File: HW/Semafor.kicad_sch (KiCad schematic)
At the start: 27 parts, among them J1 USB_C_Receptacle_USB2.0, U1 ESP32-C3

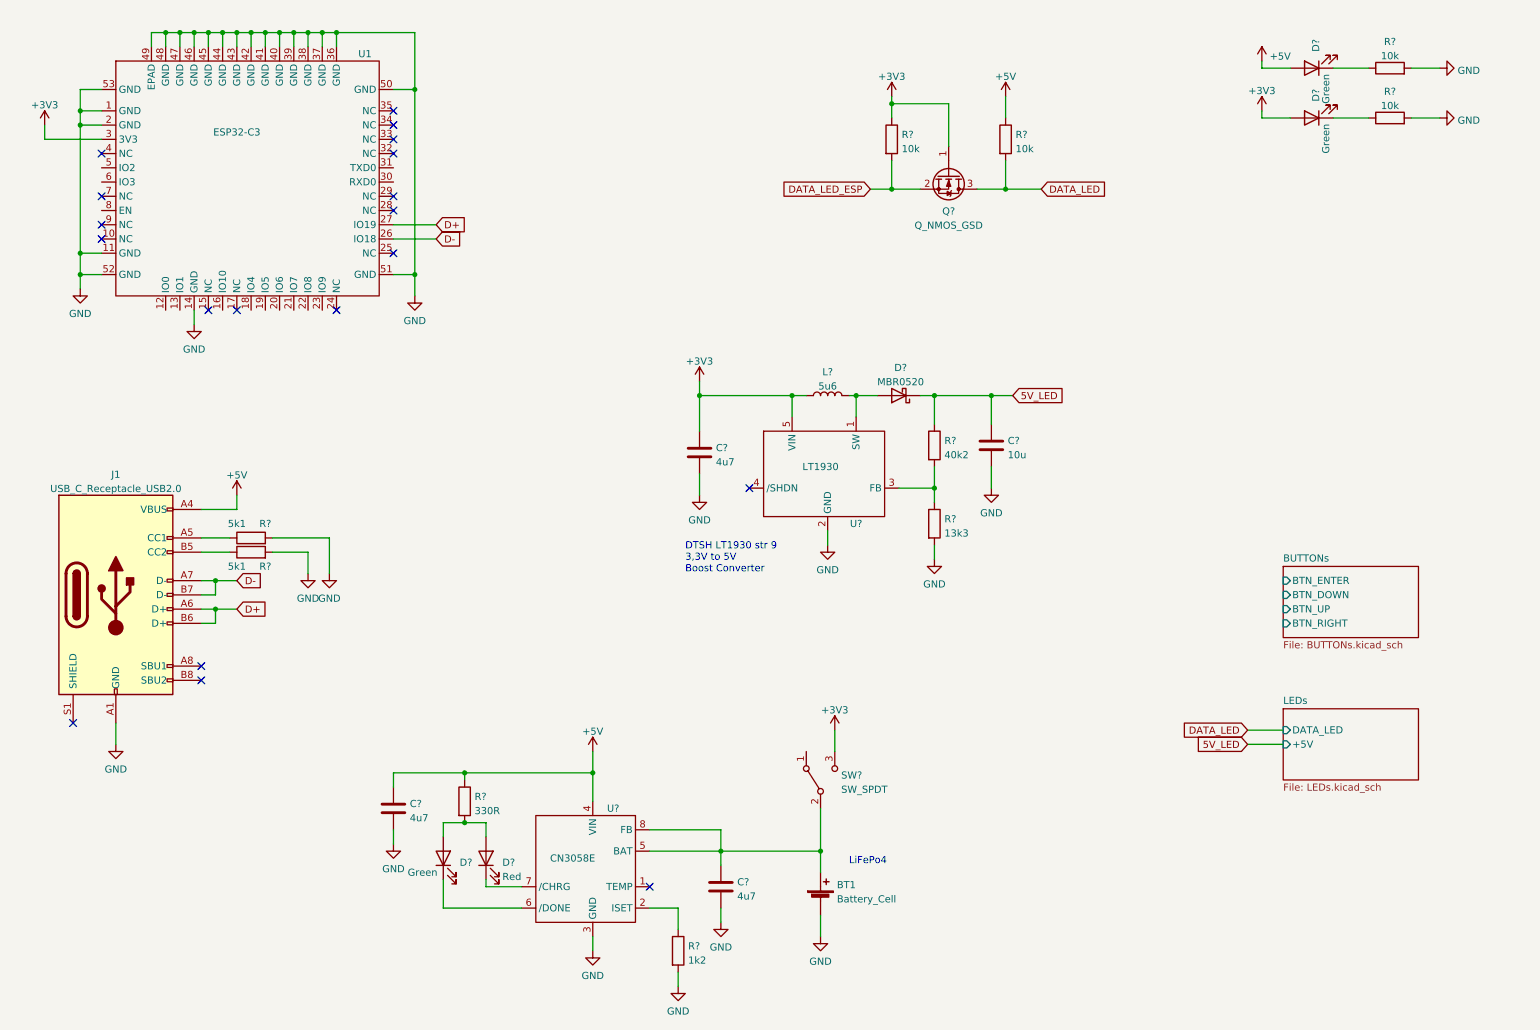
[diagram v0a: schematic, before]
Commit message: add peripherial for ESP32-C3, add temporary package of switch and inductor, add package of MOS
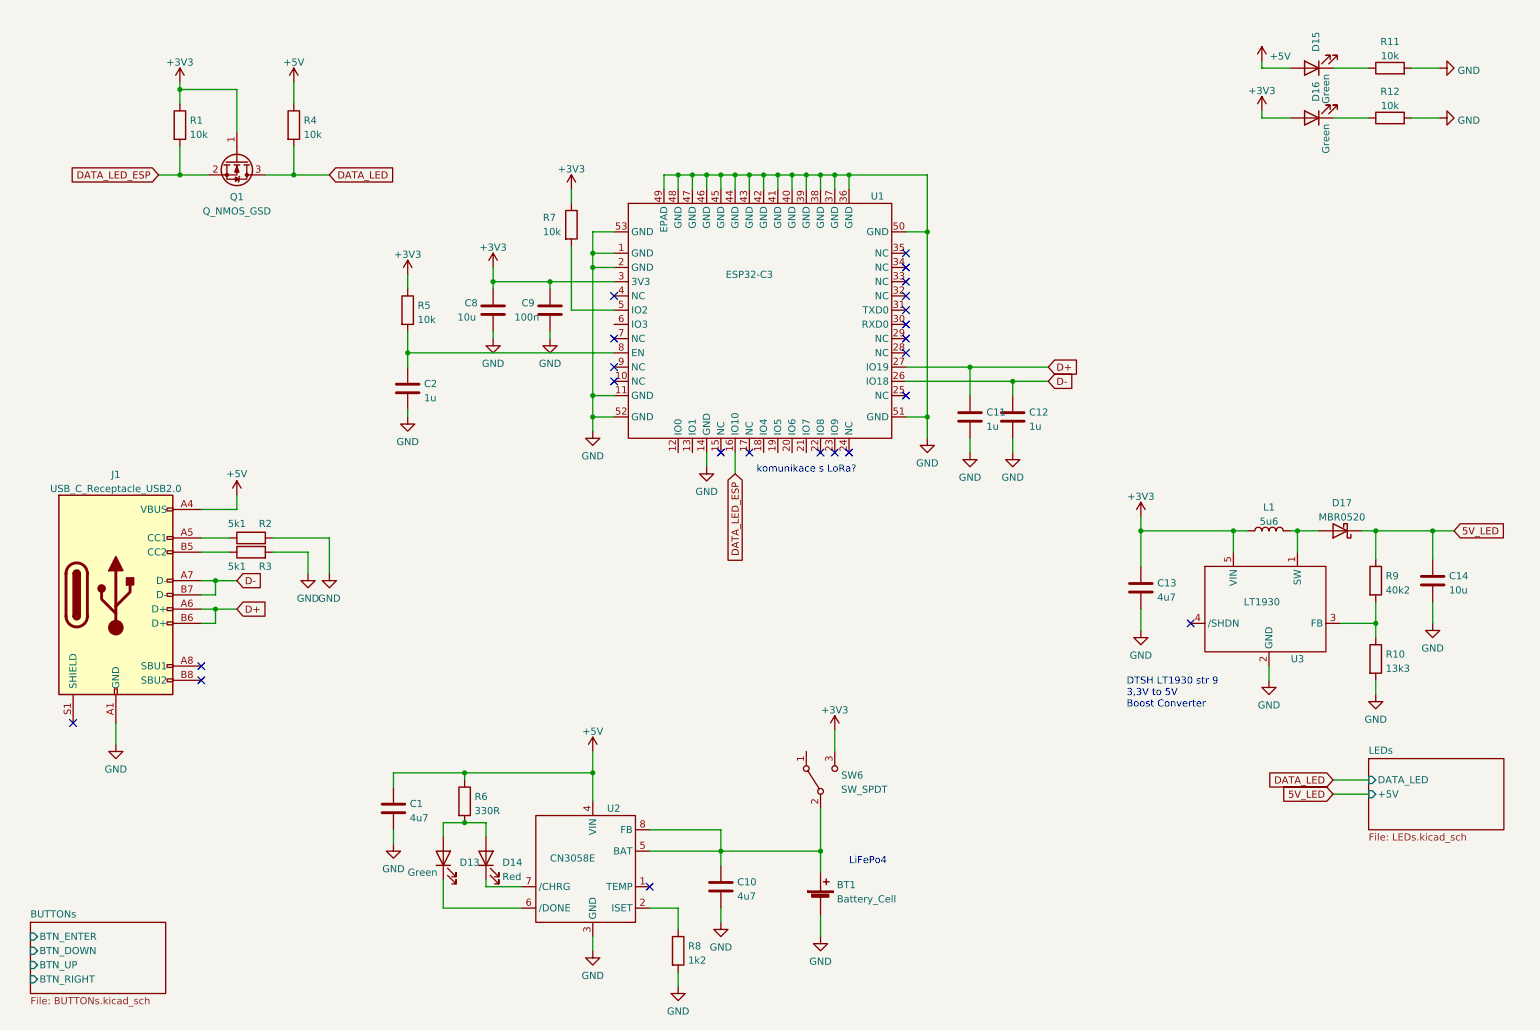
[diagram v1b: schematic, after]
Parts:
- added C11, C12, C2: 1u, Capacitor_SMD:C_0805_2012Metric, symbol Device:C
- added C8: 10u, Capacitor_SMD:C_0805_2012Metric, symbol Device:C
- added C9: 100n, Capacitor_SMD:C_0805_2012Metric, symbol Device:C
- added R5, R7: 10k, Resistor_SMD:R_0603_1608Metric, symbol Device:R
- L1: renamed from L?; footprint (none) -> Inductor_SMD:L_6.3x6.3_H3
- Q1: renamed from Q?; footprint (none) -> Package_TO_SOT_SMD:SOT-23; LCSC (none) -> C8545
- SW6: renamed from SW?; footprint (none) -> Connector_PinSocket_2.54mm:PinSocket_1x03_P2.54mm_Vertical
- gave numbers to parts that had none: 21
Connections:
- net +3V3: now also C8.1, C9.1, R5.1, R7.1
- net D+: now also C11.1
- net D-: now also C12.1
- net DATA_LED_ESP: now also U1.16 (IO10)
- net GND: now also C11.2, C12.2, C2.2, C8.2, C9.2
- net at U1.5 (IO2): now also R7.2
- net at U1.8 (EN): now also C2.1, R5.2
- no-connect marks 19 -> 23
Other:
- note added: "komunikace s LoRa?"
- moved on the sheet: C13, C14, D17, L1, Q1, R1, R10, R4, R9, U1, U3

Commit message: change package of inductor + add LSCS code
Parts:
- L1: LCSC (none) -> C167273
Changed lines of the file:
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@@
+      (effects (font (size 1.27 1.27)) hide)
+    )
+    (property "LCSC" "C167273" (id 4) (at 238.76 107.95 0)
       (effects (font (size 1.27 1.27)) hide)
     )

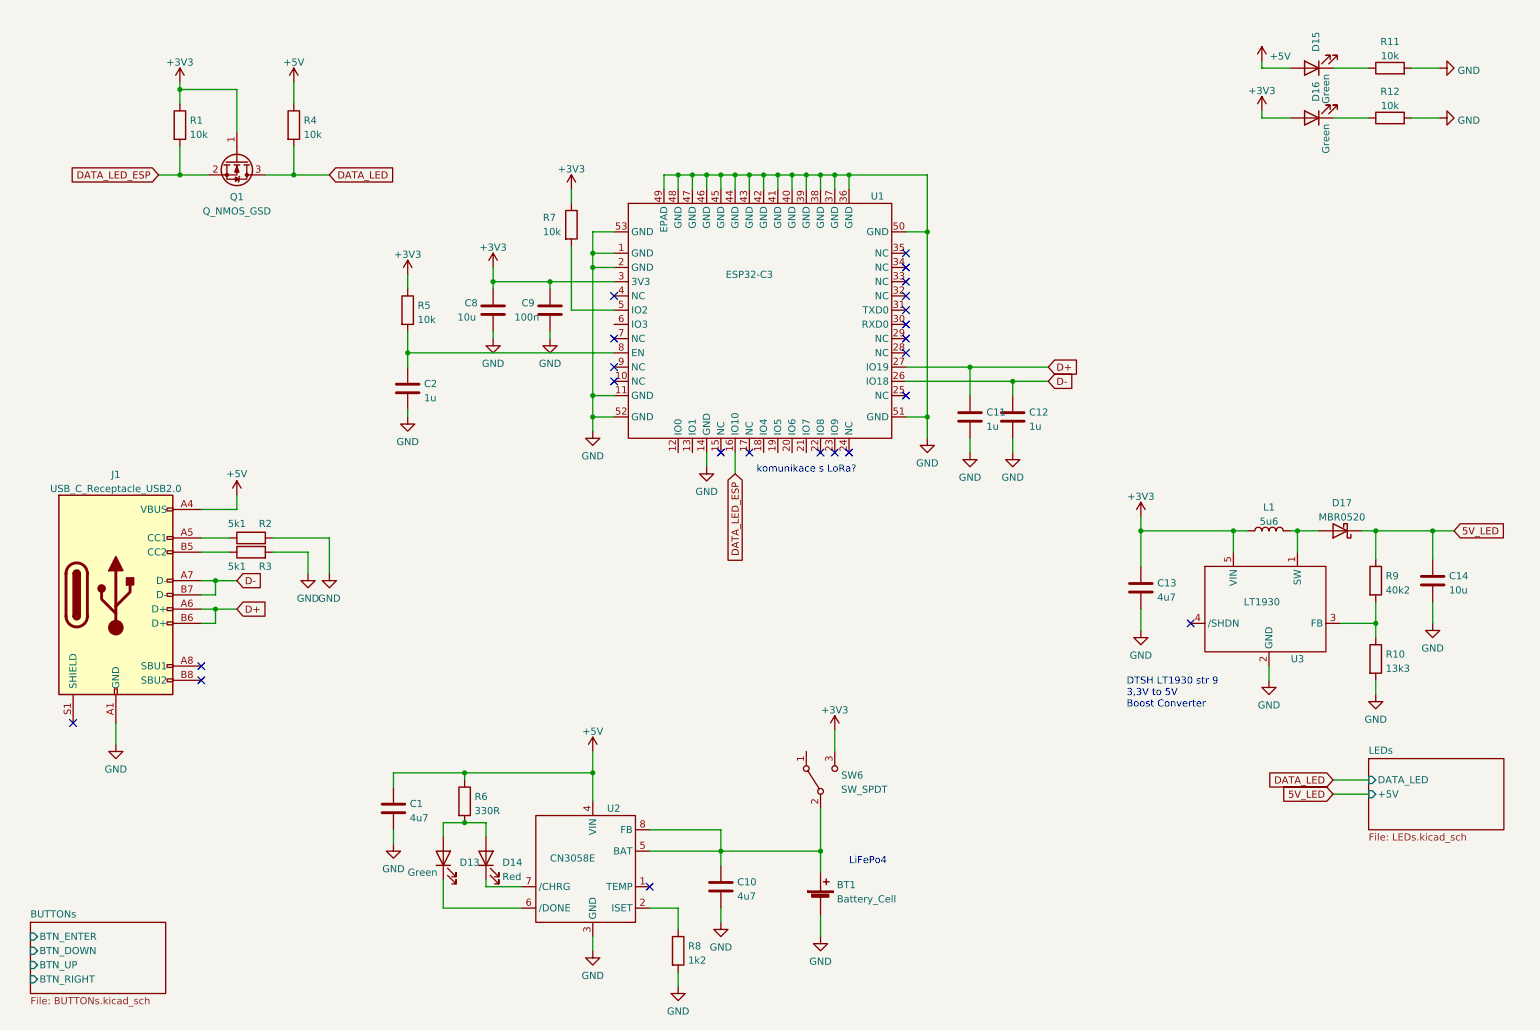
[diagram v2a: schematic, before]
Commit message: change value of inductor, update PCB, repair connection step up of pin /SHDN, delete capacitors from ESP32
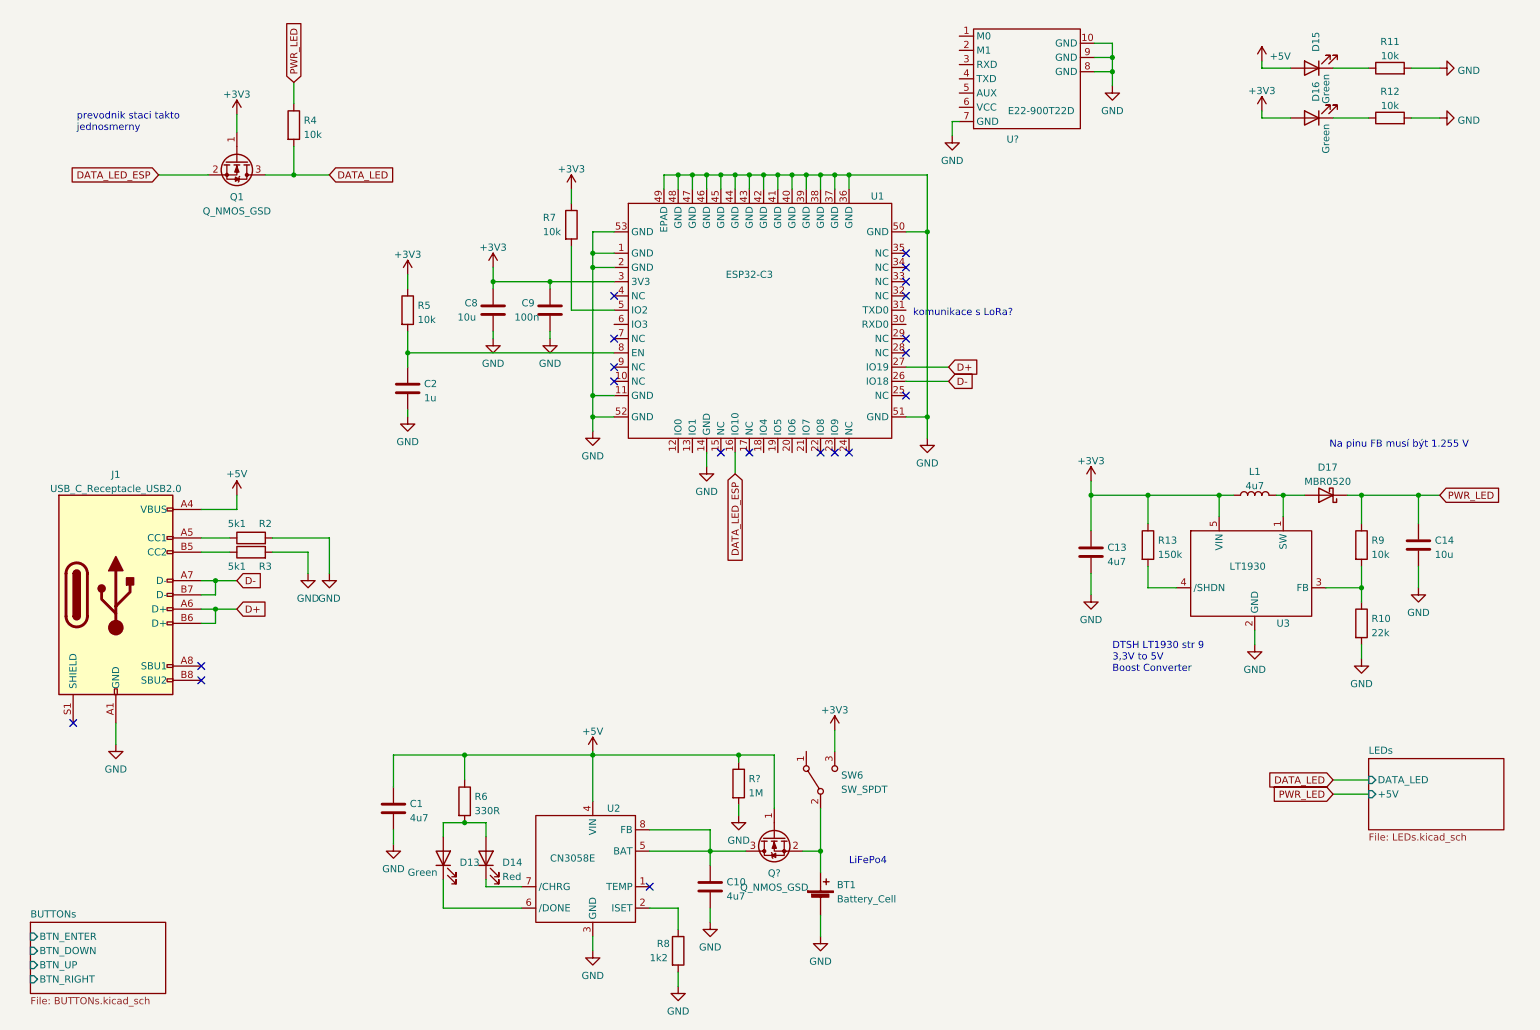
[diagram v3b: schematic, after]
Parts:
- removed C11, C12: 1u, Capacitor_SMD:C_0805_2012Metric, symbol Device:C
- removed R1: 10k, Resistor_SMD:R_0603_1608Metric, symbol Device:R
- added Q?: Q_NMOS_GSD, Package_TO_SOT_SMD:SOT-23, symbol Device:Q_NMOS_GSD
- added R13: 150k, Resistor_SMD:R_0603_1608Metric, symbol Device:R
- added R?: 1M, Resistor_SMD:R_0603_1608Metric, symbol Device:R
- added U?: E22-900T22D, Library:E22-900T22D, symbol Library:E22-900T22D
- L1: value 5u6 -> 4u7; footprint Inductor_SMD:L_6.3x6.3_H3 -> Library:L_CDRH3D18
- R10: value 13k3 -> 22k
- R9: value 40k2 -> 10k
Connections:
- net +3V3: now also R13.1
- net +5V: now also Q?.1 (G), R?.1; no longer R4.1
- net GND: now also R?.2, U?.10 (GND), U?.7 (GND), U?.8 (GND), U?.9 (GND)
- net at U3.4 (/SHDN): now also R13.2
- net at C10.1, U2.5 (BAT), U2.8 (FB): now also Q?.3 (D); no longer BT1.1 (+), SW6.2 (B)
- net 5V_LED renamed PWR_LED
- net PWR_LED: now also R4.1
- new net: BT1.1 (+), Q?.2 (S), SW6.2 (B)
- no-connect marks 23 -> 20
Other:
- note added: "Na pinu FB musí být 1.255 V"
- note added: "prevodnik staci takto jednosmerny"
- moved on the sheet: C10, C13, C14, D17, L1, R10, R9, U3

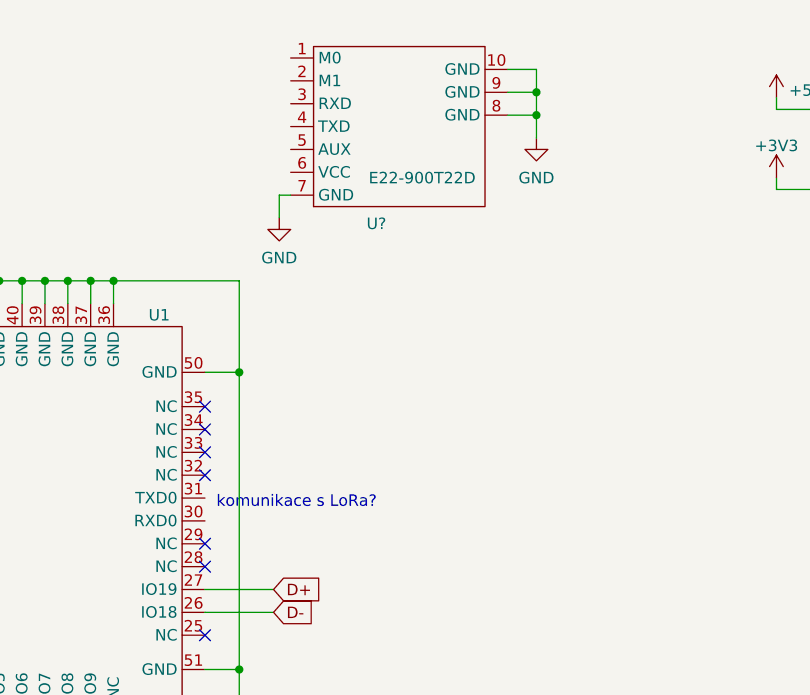
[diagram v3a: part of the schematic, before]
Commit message: update symbol of LoRa module
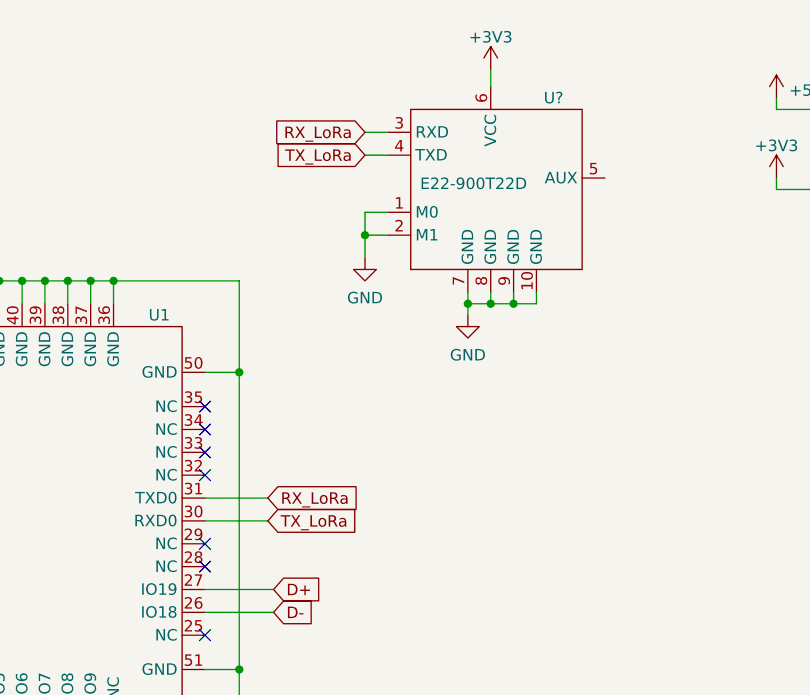
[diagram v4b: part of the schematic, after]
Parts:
- removed U?: E22-900T22D, Library:E22-900T22D, symbol Library:E22-900T22D
- added U?: E22-900T22D, symbol Library:E22-900T22D
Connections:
- net +3V3: now also U?.6 (VCC)
- net GND: now also U?.1 (M0), U?.10 (GND), U?.2 (M1), U?.7 (GND), U?.8 (GND), U?.9 (GND)
- net TX_LoRa: now reaches U1.30 (RXD0)
- net TX_LoRa: now also U?.4 (TXD)
- net RX_LoRa: now reaches U1.31 (TXD0)
- net RX_LoRa: now also U?.3 (RXD)
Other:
- note removed: "komunikace s LoRa?"
